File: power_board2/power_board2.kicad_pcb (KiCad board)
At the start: 2 copper layers, 70 x 100 mm, 67 parts, among them IC1 ADP3338AKCZ-5-REEL, IC2 PJ-002A, J1 UJC-HP-3-SMT-TR, J2 Conn_01x04, J3 Conn_01x04, J4 Conn_01x02, K1 Relay_SPDT, Q1 NMOS, U1 NUCLEO-F303K8, U2 MCP2551-I-SN, U3 ACS770xCB-100U-PFF

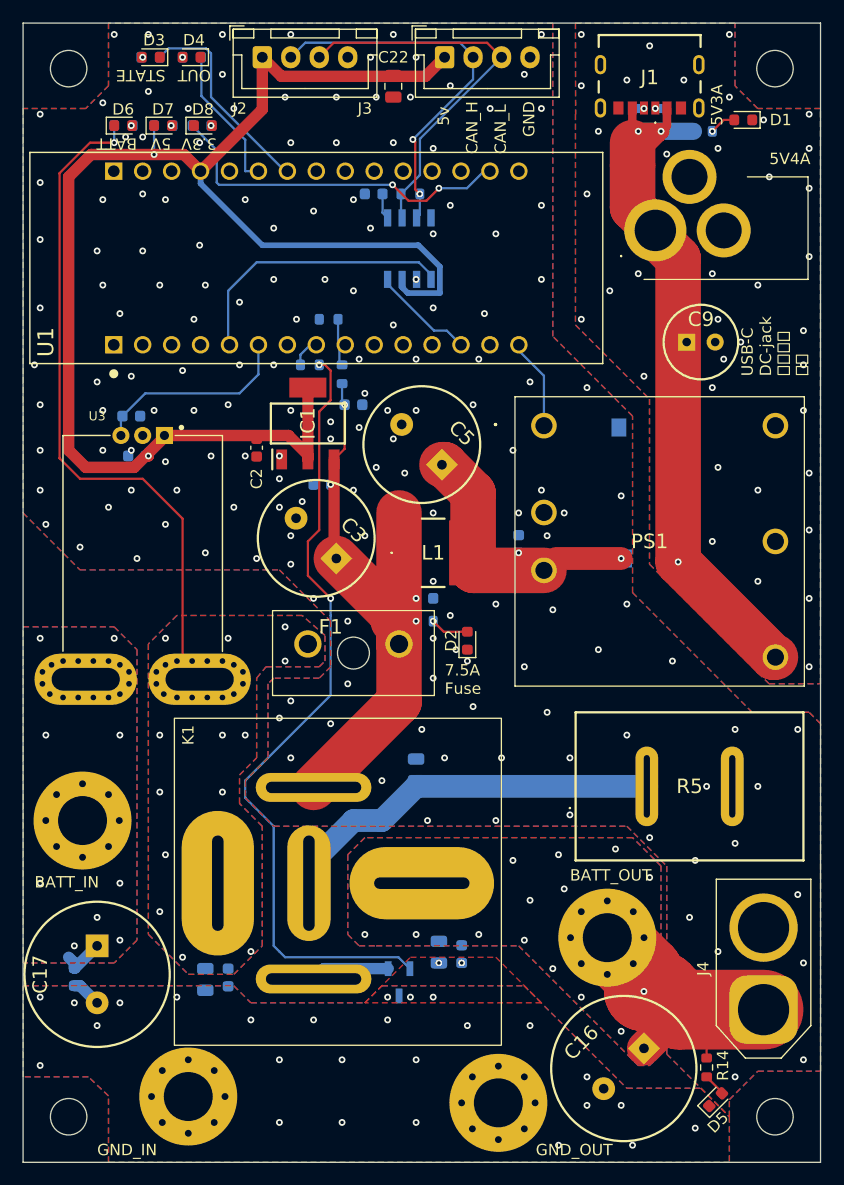
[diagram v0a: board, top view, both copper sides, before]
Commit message: 非常停止スイッチを追加
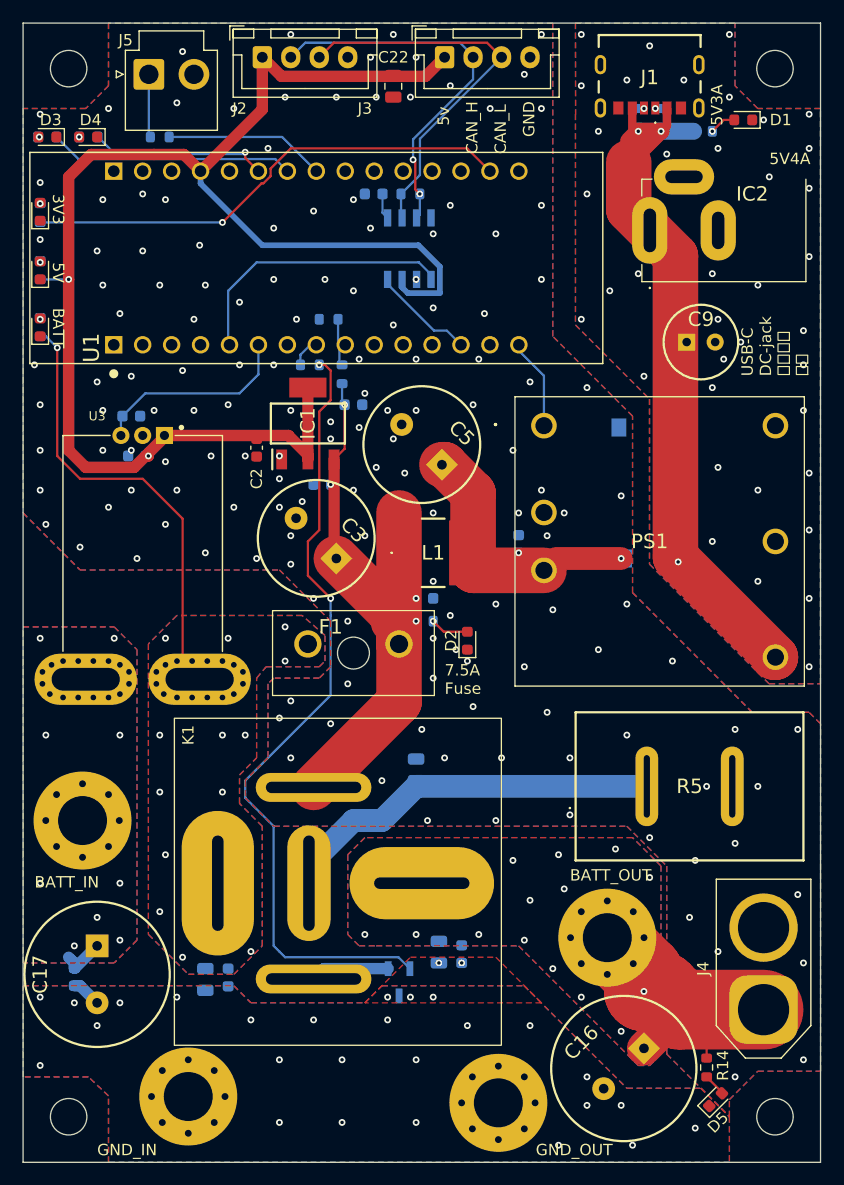
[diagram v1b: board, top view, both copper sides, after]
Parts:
- added J5: Conn_01x02, Connector_JST:JST_VH_B2P-VH_1x02_P3.96mm_Vertical, F.Cu at (66.0, 81.5)
- added R8: 1.5k, Resistor_SMD:R_0603_1608Metric, B.Cu at (67.0, 87.0)
- IC2: footprint power_board2:PJ002A -> power_board2:PJ002AH
- R1, R16: value 150 -> 1.5k
- R12, R13, R17: value 68 -> 1.5k
- R15: value 680 -> 10k
- moved D6 19.2 mm to (56.5, 103.7), turned to 90 degrees
- moved R15 19.1 mm to (56.5, 103.7), turned to 90 degrees
- moved D7 16.7 mm to (56.5, 98.7), turned to 90 degrees
- moved R16 16.7 mm to (56.5, 98.7), turned to 90 degrees
- moved D8 16.2 mm to (56.5, 93.6), turned to 90 degrees
- moved R17 16.1 mm to (56.5, 93.7), turned to 90 degrees
- moved D3 11.5 mm to (57.1, 87.0)
- moved R13 11.5 mm to (60.8, 87.0)
- moved D4 11.5 mm to (60.7, 87.0)
- moved R12 11.5 mm to (57.1, 87.0)
- moved IC2 0.48 mm to (110.0, 95.2), turned to 0 degrees
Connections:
- U1 pad 4_8: unconnected-(U1B-PA5-Pad4_8) -> /emergency_switch
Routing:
- net +BATT_FOR_MOTOR: track 59.4 -> 38.7 mm
- net /emergency_switch: track 0.00 -> 14.2 mm
- net +3V3: track 31.1 -> 43.4 mm, vias 2 -> 1
- net Net-(J5-Pin_1): track 0.00 -> 5.56 mm
- net /emergency_LED: track 12.2 -> 15.8 mm, vias 0 -> 1
- net /state_LED: track 18.2 -> 21.5 mm
- net +5VA: track 68.5 -> 66.5 mm
- net GND: vias 192 -> 180
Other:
- rule pad_to_mask_clearance: 0 -> 0.1
- board text added: "3V3"
- board text removed: "3.3V"
- board text removed: "OUT"
- board text removed: "STATE"
